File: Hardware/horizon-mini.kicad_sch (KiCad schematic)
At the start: 81 parts, among them J15 arming terminal, J16 arming terminal, J2 Conn_01x02_Pin, J3 Micro_SD_Card_Det1, J7 USB_C_Receptacle_USB2.0_16P, J8 Conn_02x03_Counter_Clockwise, Q1 BSS138, Q10 DMG2301L, U1 TPS82130, U16 AP2112K-3.3, U2 TPS61092, U3 LTC4412xS6, U5 ATSAMD21G18A-A, U6 NAND, U7 LPS22HB, U9 LSM6DS3

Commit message: please look it over, I'm finished with it
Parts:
- removed J15: arming terminal, TerminalBlock_Phoenix:TerminalBlock_Phoenix_MPT-0,5-2-2.54_1x02_P2.54mm_Horizontal, symbol Connector:Screw_Terminal_01x02
- removed R78: 10k, Resistor_SMD:R_0603_1608Metric, symbol Device:R
- added D2: LED, LED_SMD:LED_0603_1608Metric, symbol Device:LED
- added F2: Polyfuse, Fuse:Fuse_0603_1608Metric, symbol Device:Polyfuse
- added J1: Screw_Terminal_01x02, TerminalBlock_Phoenix:TerminalBlock_Phoenix_MPT-0,5-2-2.54_1x02_P2.54mm_Horizontal, symbol Connector:Screw_Terminal_01x02
- added Q2: IRLML6402, Package_TO_SOT_SMD:SOT-23, symbol Transistor_FET:IRLML6402
- added R30: 100, Resistor_SMD:R_0603_1608Metric, symbol Device:R
- added R31: 1k, Resistor_SMD:R_0603_1608Metric, symbol Device:R
- J16: symbol Connector:Screw_Terminal_01x02 -> Connector_Generic:Conn_01x02
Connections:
- net GND: now also F2.2
- net mosfet1_signalfire: now reaches U5.9 (PA04)
- net mosfet1_signalfire: now also R30.1
- net at R80.2: now also Q2.3 (D), R31.2
- new net: D2.1 (K), J1.1 (Pin_1), Q2.2 (S)
- new net: D2.2 (A), R31.1
- new net: F2.1, J1.2 (Pin_2)
- new net: Q2.1 (G), R30.2
- no-connect marks 29 -> 28
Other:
- moved on the sheet: R29, R80

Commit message: forgot to push from last night. Very small silscreen changes and stuff
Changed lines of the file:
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@@
 		(on_board yes)
 		(dnp no)
-		(fields_autoplaced yes)
 		(property "Reference" "#PWR041"
 			(at 154.94 247.65 0)
@@
 		)
 		(property "Value" "+3.3V"
-			(at 154.9401 240.03 90)
+			(at 156.972 243.586 90)
 			(effects
 				(font

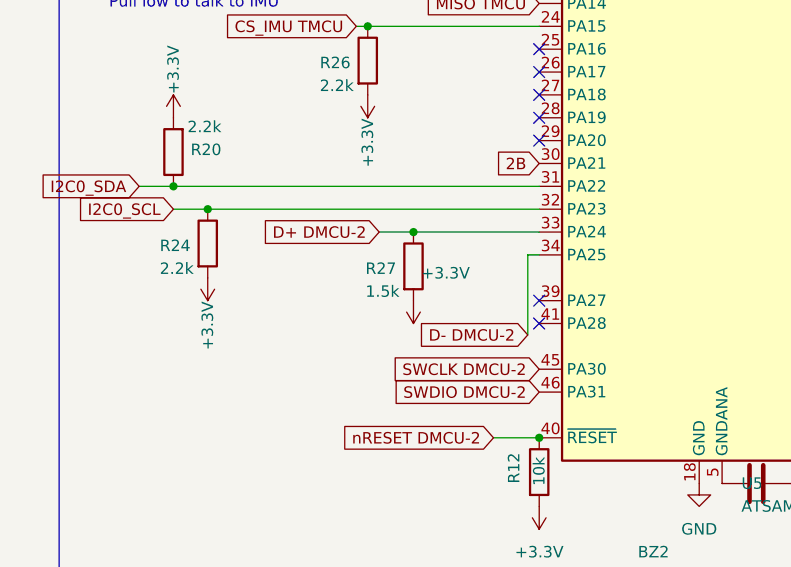
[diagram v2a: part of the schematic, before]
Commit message: fixed the data lines. @mpkendall please review so we don't need x3 :)
no gerber's were exported for this.
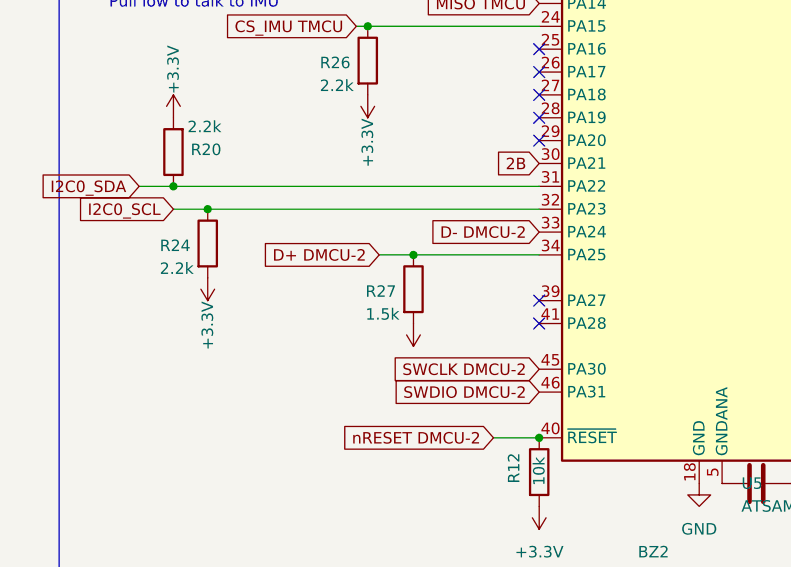
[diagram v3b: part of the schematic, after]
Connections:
- net D+ DMCU-2: now also U5.34 (PA25); no longer U5.33 (PA24)
- net D- DMCU-2: now also U5.33 (PA24); no longer U5.34 (PA25)

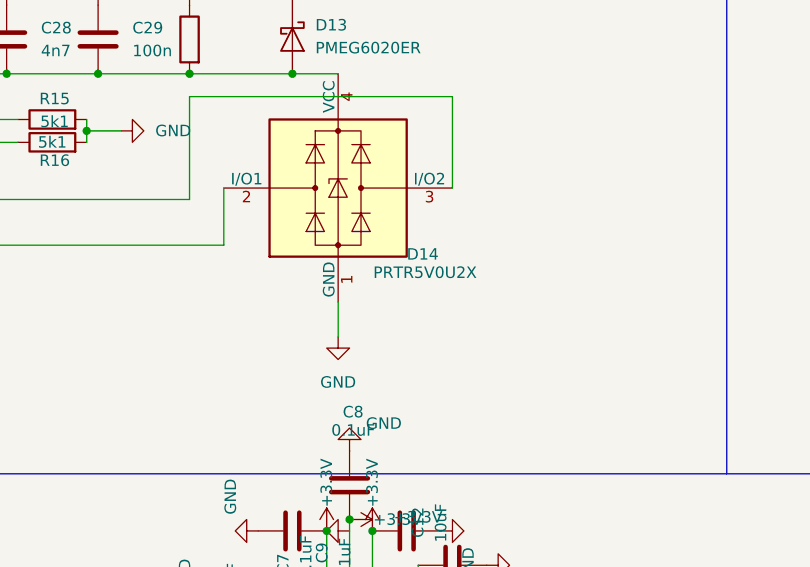
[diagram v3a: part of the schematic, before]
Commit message: @starry-liam please re-gen gerbers: fixed schematic parity
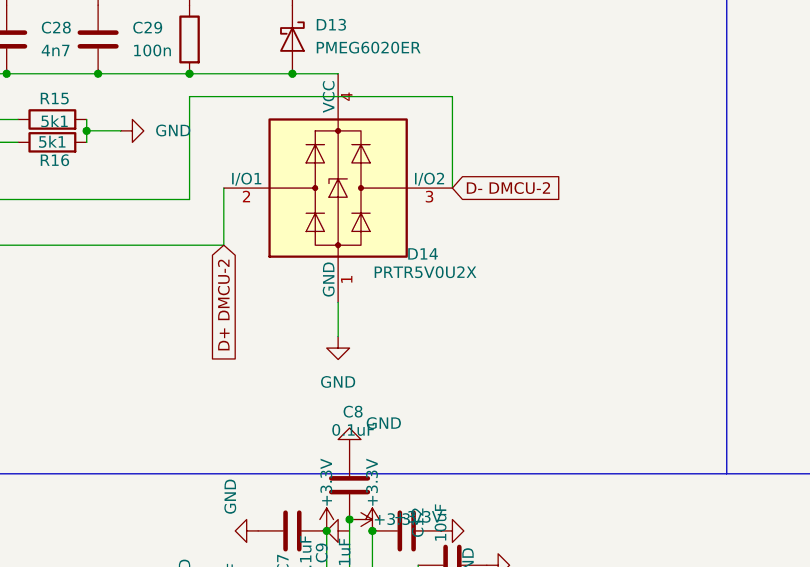
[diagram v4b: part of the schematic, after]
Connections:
- net D+ DMCU-2: now also D14.2 (I/O1), J7.A6 (D+), J7.B6 (D+)
- net D- DMCU-2: now also D14.3 (I/O2), J7.A7 (D-), J7.B7 (D-)
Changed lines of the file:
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@@
+		)
+	)
+	(global_label "D+ DMCU-2"
+		(shape input)
+		(at 69.85 50.8 270)
+		(fields_autoplaced yes)
+		(effects
+			(font
+				(size 1.27 1.27)
+			)
+			(justify right)
+		)
+		(property "Intersheetrefs" "${INTERSHEET_REFS}"
+			(at 69.85 65.699 90)
+			(hide yes)
+			(effects
+				(font
+					(size 1.27 1.27)
+				)
+				(justify right)
+			)
 		)
 	)
@@
 			)
 		)
+	)
+	(global_label "D- DMCU-2"
+		(shape input)
+		(at 95.25 44.45 0)
+		(fields_autoplaced yes)
+		(effects
+			(font
+				(size 1.27 1.27)
+			)
+			(justify left)
+		)
+		(property "Intersheetrefs" "${INTERSHEET_REFS}"
+			(at 110.149 44.45 0)
+			(hide yes)
+			(effects
+				(font
+					(size 1.27 1.27)
+				)
+				(justify left)
+			)
+		)

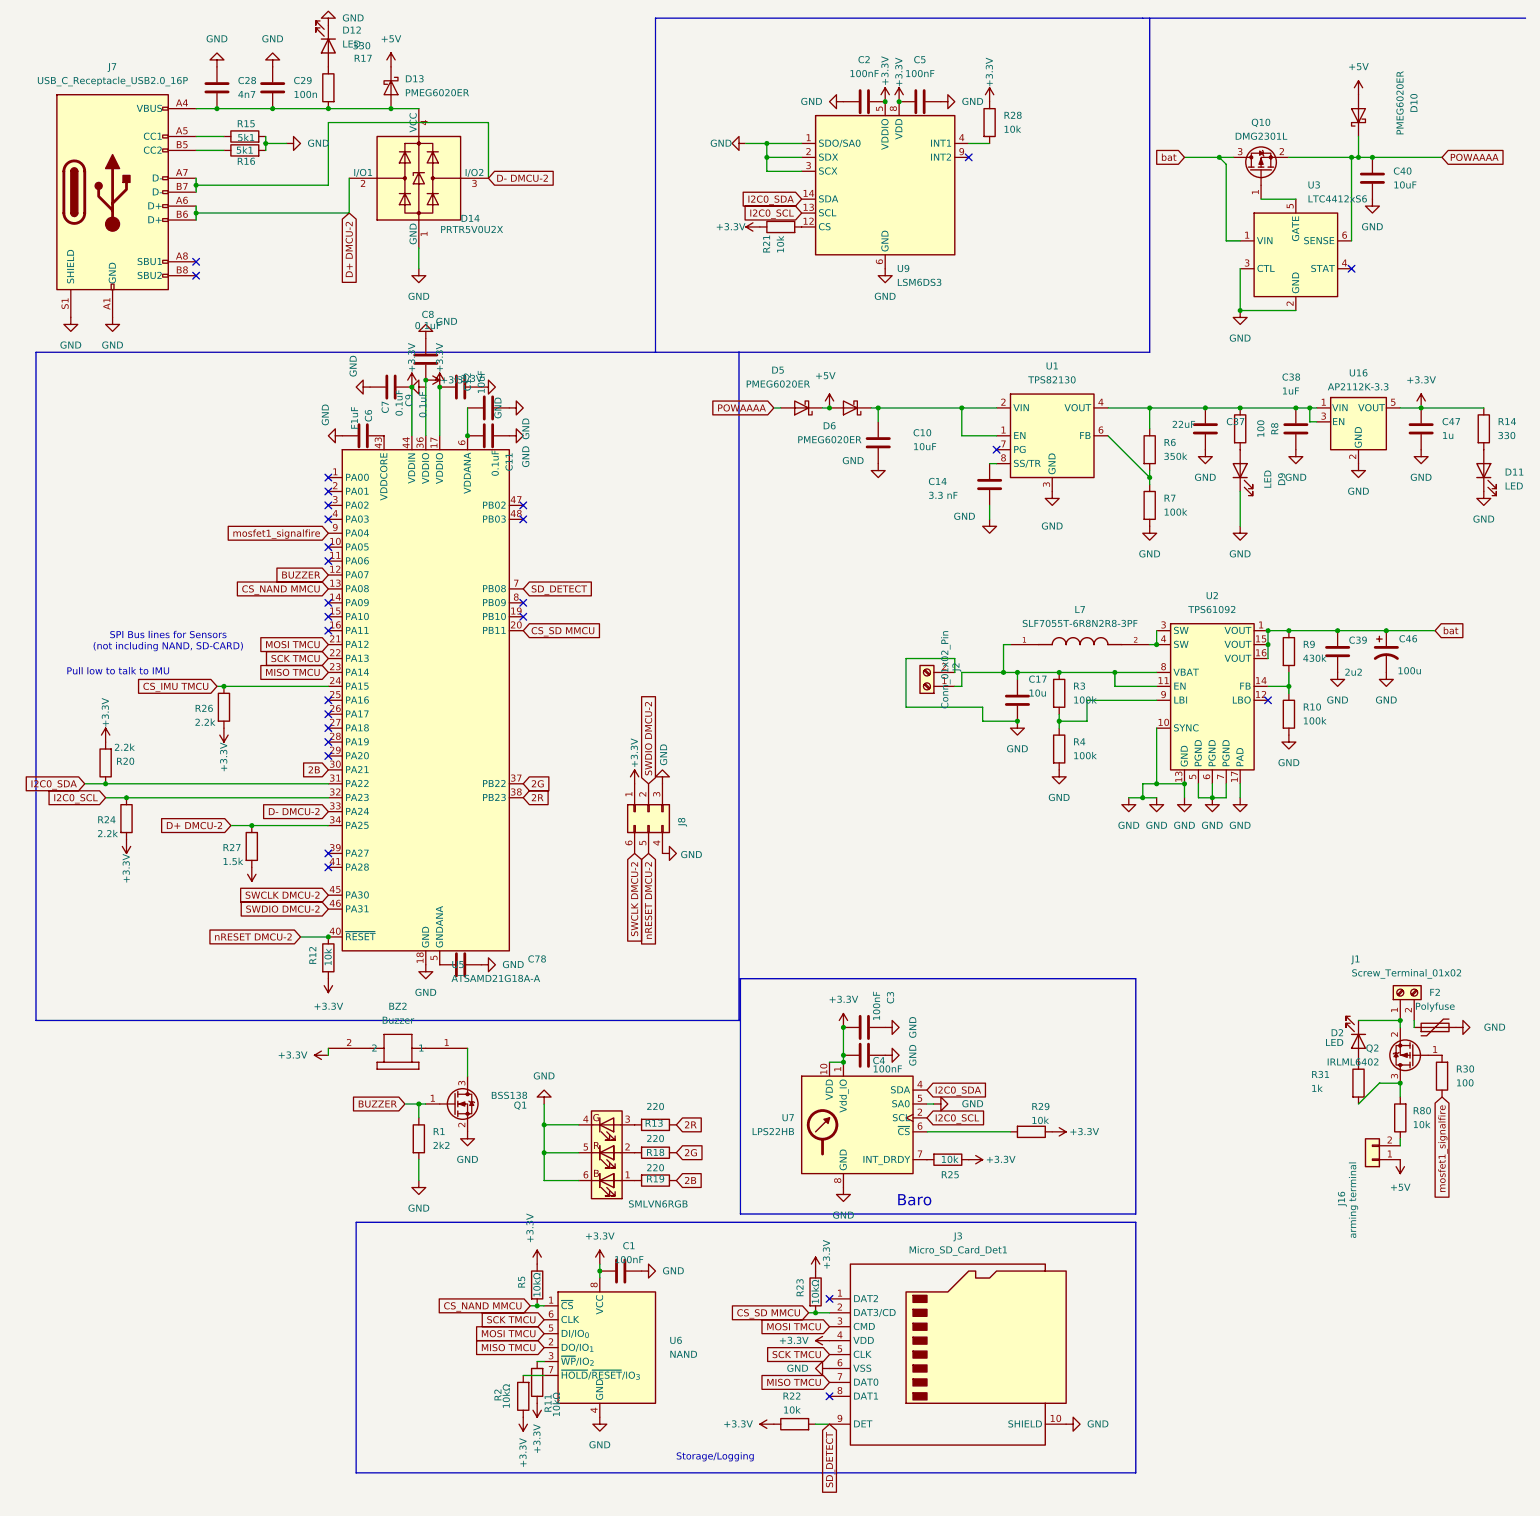
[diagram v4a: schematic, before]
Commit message: Changed the Baro to the higher accuracy one, and worked on re-doing the pyro-output... almost done it!
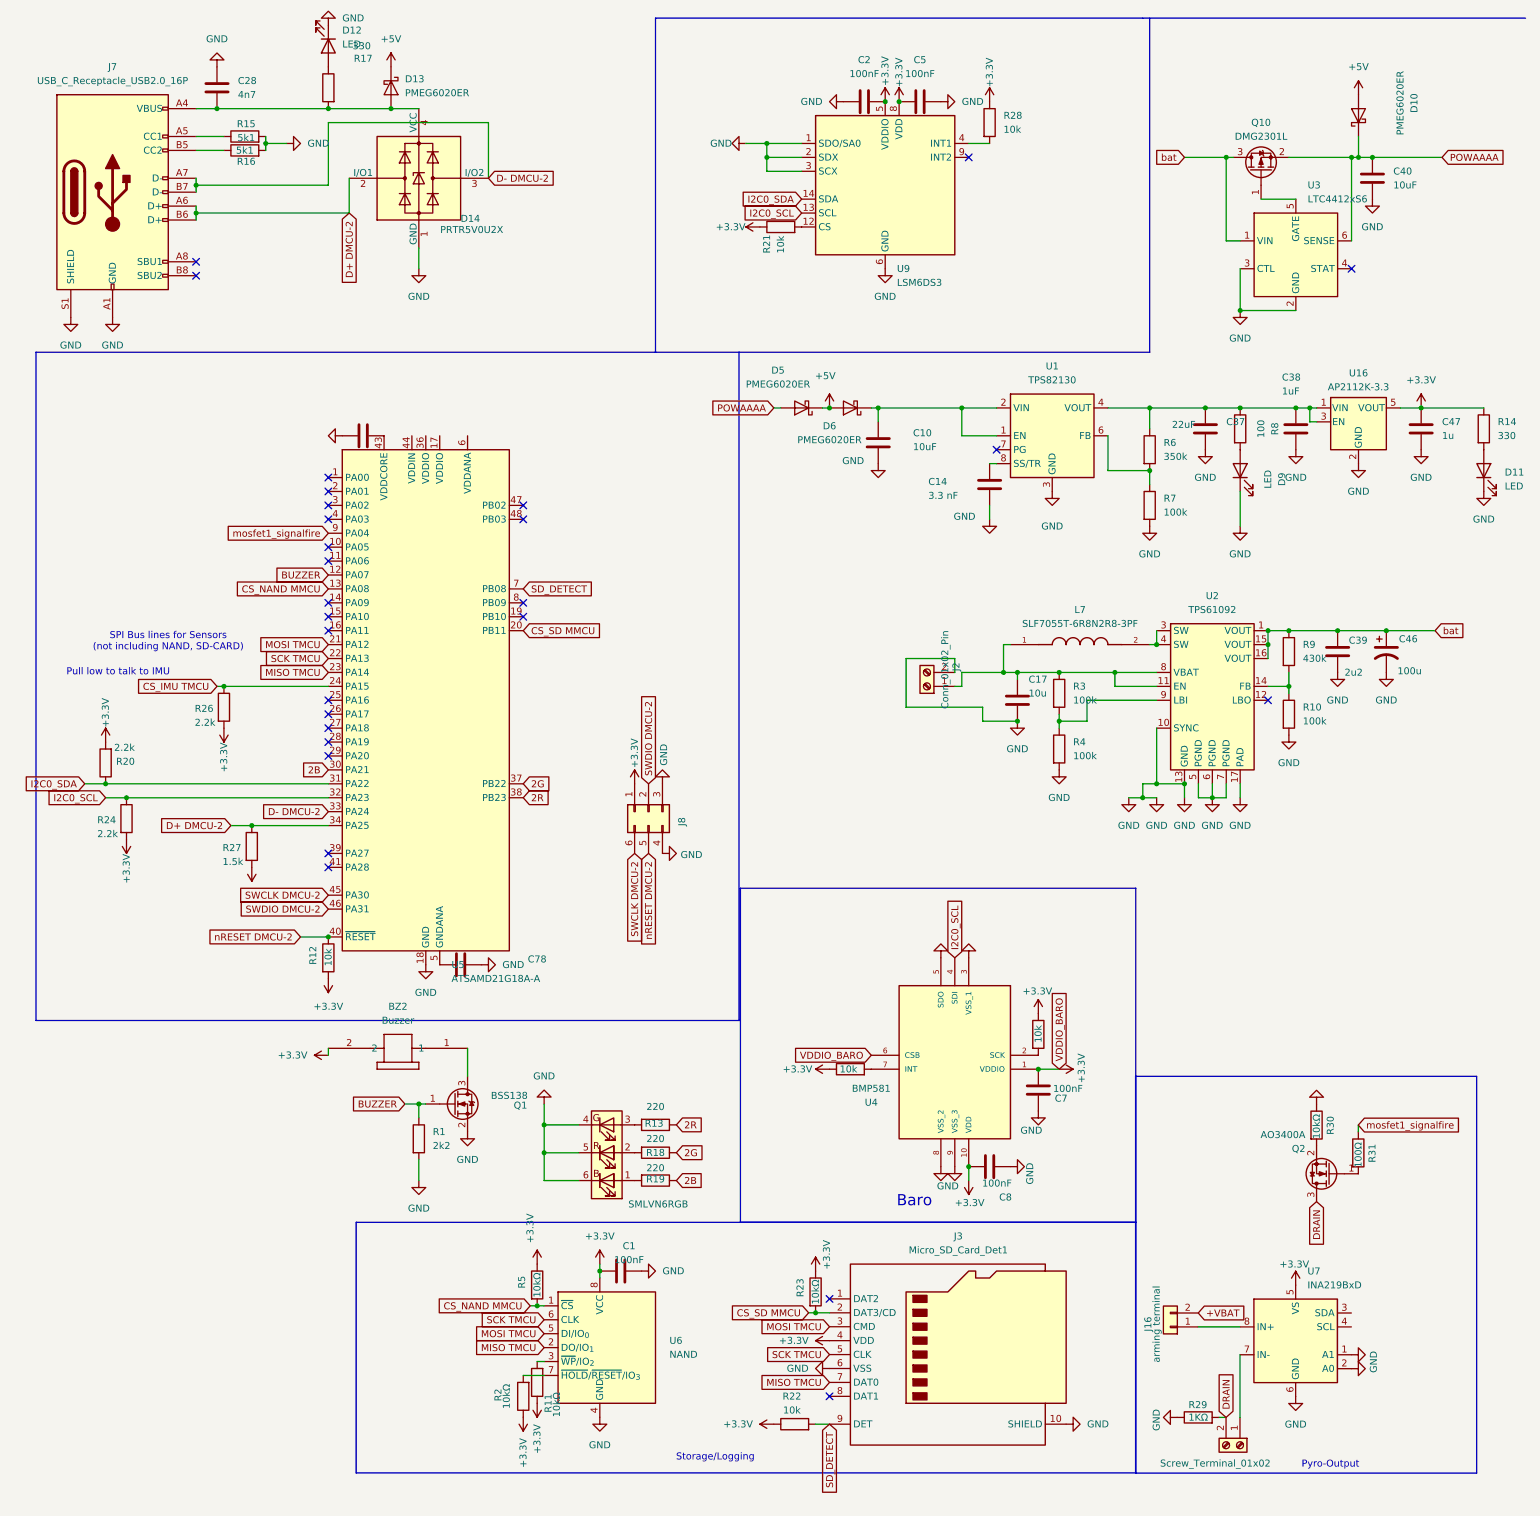
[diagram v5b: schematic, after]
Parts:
- removed C11, C9: 0.1uF, Capacitor_SMD:C_0603_1608Metric, symbol Device:C
- removed C12: 10uF, Capacitor_SMD:C_0603_1608Metric, symbol Device:C
- removed C29: 100n, Capacitor_SMD:C_0603_1608Metric, symbol Device:C
- removed C3, C4: 100nF, Capacitor_SMD:C_0603_1608Metric, symbol Device:C
- removed D2: LED, LED_SMD:LED_0603_1608Metric, symbol Device:LED
- removed F2: Polyfuse, Fuse:Fuse_0603_1608Metric, symbol Device:Polyfuse
- removed J1: Screw_Terminal_01x02, TerminalBlock_Phoenix:TerminalBlock_Phoenix_MPT-0,5-2-2.54_1x02_P2.54mm_Horizontal, symbol Connector:Screw_Terminal_01x02
- removed Q2: IRLML6402, Package_TO_SOT_SMD:SOT-23, symbol Transistor_FET:IRLML6402
- removed R25, R80: 10k, Resistor_SMD:R_0603_1608Metric, symbol Device:R
- removed U7: LPS22HB, Package_LGA:ST_HLGA-10_2x2mm_P0.5mm_LayoutBorder3x2y, symbol Sensor_Pressure:LPS22HB
- added J4: Screw_Terminal_01x02, TerminalBlock_Phoenix:TerminalBlock_Phoenix_MPT-0,5-2-2.54_1x02_P2.54mm_Horizontal, symbol Connector:Screw_Terminal_01x02
- added Q2: AO3400A, Package_TO_SOT_SMD:SOT-23, symbol Transistor_FET:AO3400A
- added R32, R33: 10k, Resistor_SMD:R_0603_1608Metric, symbol Device:R
- added U4: BMP581, BMP581:BMP581, symbol BMP581:BMP581
- added U7: INA219BxD, Package_SO:SOIC-8_3.9x4.9mm_P1.27mm, symbol Sensor_Energy:INA219BxD
- C7, C8: value 0.1uF -> 100nF; footprint Capacitor_SMD:C_0603_1608Metric -> (none)
- R29: value 10k -> 1KΩ; footprint Resistor_SMD:R_0603_1608Metric -> (none)
- R30: value 100 -> 10kΩ; footprint Resistor_SMD:R_0603_1608Metric -> (none)
- R31: value 1k -> 100Ω; footprint Resistor_SMD:R_0603_1608Metric -> (none)
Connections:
- net +3.3V: now also R32.1, R33.1, U4.1 (VDDIO), U4.10 (VDD), U4.6 (CSB), U7.5 (VS); no longer R29.1, U5.17 (VDDIO), U5.36 (VDDIO), U5.44 (VDDIN)
- net +5V: no longer J16.1 (Pin_1)
- net GND: now also R29.1, R30.1, U4.3 (VSS_1), U4.5 (SDO), U4.8 (VSS_2), U4.9 (VSS_3), U7.1 (A1), U7.2 (A0), U7.6 (GND)
- net I2C0_SCL: now also U4.4 (SDI)
- net mosfet1_signalfire: now also R31.1; no longer R30.1
- net +VBAT: now reaches J16.2 (Pin_2)
- net at R31.2: now also Q2.1 (G)
- net DRAIN: now reaches R29.2
- net DRAIN: now also J4.2 (Pin_2), Q2.3 (D)
- net at R30.2: now also Q2.2 (S)
- new net: R33.2, U4.7 (INT)
- new net: J4.1 (Pin_1), U7.7 (IN-)
- new net: J16.1 (Pin_1), U7.8 (IN+)
- new net: R32.2, U4.2 (SCK)
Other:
- note added: "Pyro-Output"
